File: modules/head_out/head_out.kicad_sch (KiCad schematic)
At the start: 27 parts, among them J1 AudioJack3, U1 MCP6002-xSN

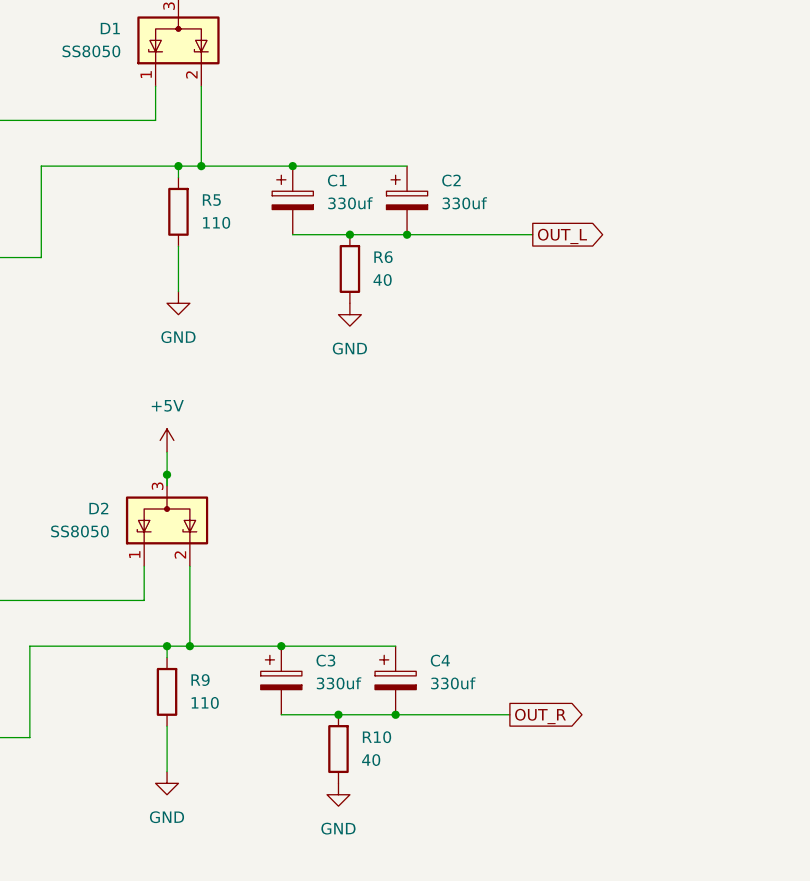
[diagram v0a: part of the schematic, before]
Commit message: Finished pcb_design of the head_out
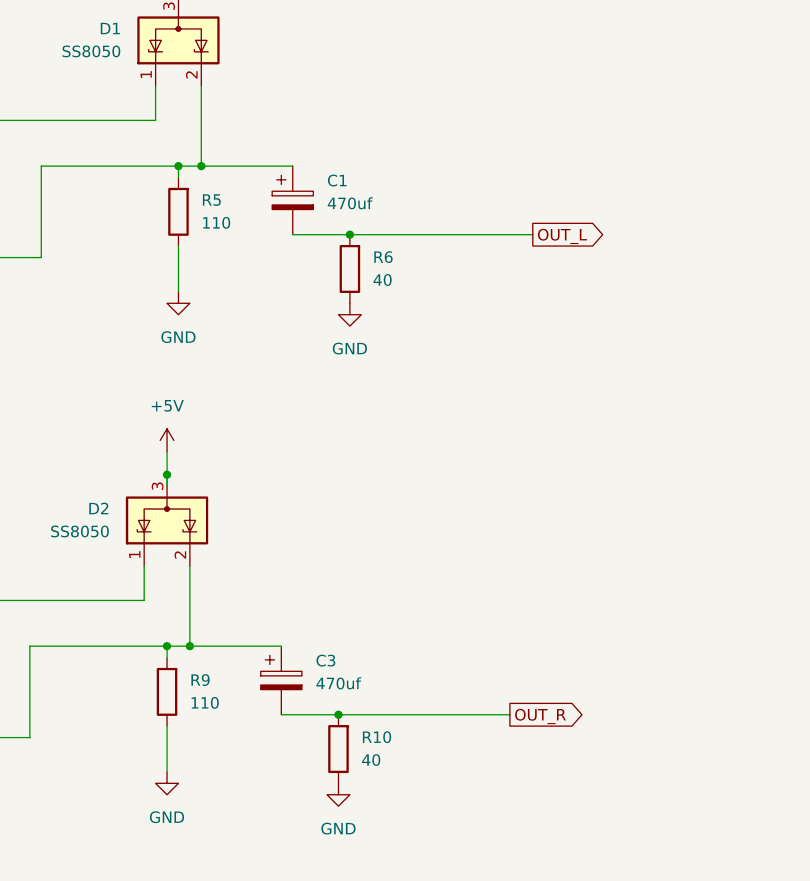
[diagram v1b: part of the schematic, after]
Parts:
- removed C2, C4: 330uf, Capacitor_SMD:CP_Elec_6.3x7.7, symbol Device:C_Polarized
- C1, C3: value 330uf -> 470uf
- RV1, RV2: footprint BreadModular_Pots:PanelHole_Potentiometer_RV09 -> BreadModular_Pots:Potentiometer_RV09
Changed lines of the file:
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@@
 	(paper "A4")
 	(junction
-		(at 153.67 143.51)
-		(diameter 0)
-		(color 0 0 0 0)
-	)
-	(junction
 		(at 82.55 80.01)
 		(diameter 0)
@@
 	)
 	(junction
-		(at 140.97 135.89)
-		(diameter 0)
-		(color 0 0 0 0)
-	)
-	(junction
 		(at 261.62 30.48)
 		(diameter 0)
@@
 	)
 	(junction
-		(at 142.24 82.55)
-		(diameter 0)
-		(color 0 0 0 0)
-	)
-	(junction
-		(at 154.94 90.17)
-		(diameter 0)
-		(color 0 0 0 0)
-	)
-	(junction
 		(at 148.59 90.17)
 		(diameter 0)
@@
 	(wire
 		(pts
-			(xy 153.67 143.51) (xy 166.37 143.51)
-		)
-		(stroke
-			(width 0)
-			(type default)
-		)
-	)
-	(wire
-		(pts
 			(xy 231.14 120.65) (xy 231.14 114.3)
 		)
@@
 	(wire
 		(pts
-			(xy 140.97 135.89) (xy 153.67 135.89)
-		)
-		(stroke
-			(width 0)
-			(type default)
-		)
-	)
-	(wire
-		(pts
-			(xy 147.32 143.51) (xy 153.67 143.51)
+			(xy 147.32 143.51) (xy 166.37 143.51)
 		)
 		(stroke
@@
 	(wire
 		(pts
-			(xy 142.24 82.55) (xy 154.94 82.55)
-		)
-		(stroke
-			(width 0)
-			(type default)
-		)
-	)
-	(wire
-		(pts
 			(xy 88.9 92.71) (xy 82.55 92.71)
 		)
@@
 	(wire
 		(pts
-			(xy 154.94 90.17) (xy 168.91 90.17)
-		)
-		(stroke
-			(width 0)
-			(type default)
-		)
-	)
-	(wire
-		(pts
 			(xy 266.7 30.48) (xy 269.24 30.48)
 		)
@@
 	(wire
 		(pts
-			(xy 148.59 90.17) (xy 154.94 90.17)
+			(xy 148.59 90.17) (xy 168.91 90.17)
 		)
 		(stroke
@@
 			)
 		)
-		(property "Value" "330uf"
+		(property "Value" "470uf"
 			(at 144.78 140.0809 0)
 			(effects
@@
 	)
 	(symbol
-		(lib_id "Device:C_Polarized")
-		(at 153.67 139.7 0)
-		(unit 1)
-		(exclude_from_sim no)
-		(in_bom yes)
-		(on_board yes)
-		(dnp no)
-		(fields_autoplaced yes)
-		(property "Reference" "C4"
-			(at 157.48 137.5409 0)
-			(effects
-				(font
-					(size 1.27 1.27)
-				)
-				(justify left)
-			)
-		)
-		(property "Value" "330uf"
-			(at 157.48 140.0809 0)
-			(effects
-				(font
-					(size 1.27 1.27)
-				)
-				(justify left)
-			)
-		)
-		(property "Footprint" "Capacitor_SMD:CP_Elec_6.3x7.7"
-			(at 154.6352 143.51 0)
-			(effects
-				(font
-					(size 1.27 1.27)
-				)
-				(hide yes)
-			)
-		)
-		(property "Datasheet" "~"
-			(at 153.67 139.7 0)
-			(effects
-				(font
-					(size 1.27 1.27)
-				)
-				(hide yes)
-			)
-		)
-		(property "Description" "Polarized capacitor"
-			(at 153.67 139.7 0)
-			(effects
-				(font
-					(size 1.27 1.27)
-				)
-				(hide yes)
-			)
-		)
-		(pin "1"
-		)
-		(pin "2"
-		)
-		(instances
-			(project "head_out"
-				(path "/b63493d3-5f6d-47e3-845b-87e7090fc1ab"
-					(reference "C4")
-					(unit 1)
-				)
-			)
-		)
-	)
-	(symbol
 		(lib_id "Connector:Conn_01x05_Pin")
 		(at 238.76 34.29 90)
@@
 			)
 		)
-		(property "Footprint" "BreadModular_Pots:PanelHole_Potentiometer_RV09"
+		(property "Footprint" "BreadModular_Pots:Potentiometer_RV09"
 			(at 41.91 140.97 0)
 			(effects
@@
 	)
 	(symbol
-		(lib_id "Device:C_Polarized")
-		(at 154.94 86.36 0)
-		(unit 1)
-		(exclude_from_sim no)
-		(in_bom yes)
-		(on_board yes)
-		(dnp no)
-		(fields_autoplaced yes)
-		(property "Reference" "C2"
-			(at 158.75 84.2009 0)
-			(effects
-				(font
-					(size 1.27 1.27)
-				)
-				(justify left)
-			)
-		)
-		(property "Value" "330uf"
-			(at 158.75 86.7409 0)
-			(effects
-				(font
-					(size 1.27 1.27)
-				)
-				(justify left)
-			)
-		)
-		(property "Footprint" "Capacitor_SMD:CP_Elec_6.3x7.7"
-			(at 155.9052 90.17 0)
-			(effects
-				(font
-					(size 1.27 1.27)
-				)
-				(hide yes)
-			)
-		)
-		(property "Datasheet" "~"
-			(at 154.94 86.36 0)
-			(effects
-				(font
-					(size 1.27 1.27)
-				)
-				(hide yes)
-			)
-		)
-		(property "Description" "Polarized capacitor"
-			(at 154.94 86.36 0)
-			(effects
-				(font
-					(size 1.27 1.27)
-				)
-				(hide yes)
-			)
-		)
-		(pin "1"
-		)
-		(pin "2"
-		)
-		(instances
-			(project "head_out"
-				(path "/b63493d3-5f6d-47e3-845b-87e7090fc1ab"
-					(reference "C2")
-					(unit 1)
-				)
-			)
-		)
-	)
-	(symbol
 		(lib_id "Amplifier_Operational:MCP6002-xSN")
 		(at 93.98 77.47 0)
@@
 			)
 		)
-		(property "Footprint" "BreadModular_Pots:PanelHole_Potentiometer_RV09"
+		(property "Footprint" "BreadModular_Pots:Potentiometer_RV09"
 			(at 43.18 87.63 0)
 			(effects
@@
 			)
 		)
-		(property "Value" "330uf"
+		(property "Value" "470uf"
 			(at 146.05 86.7409 0)
 			(effects

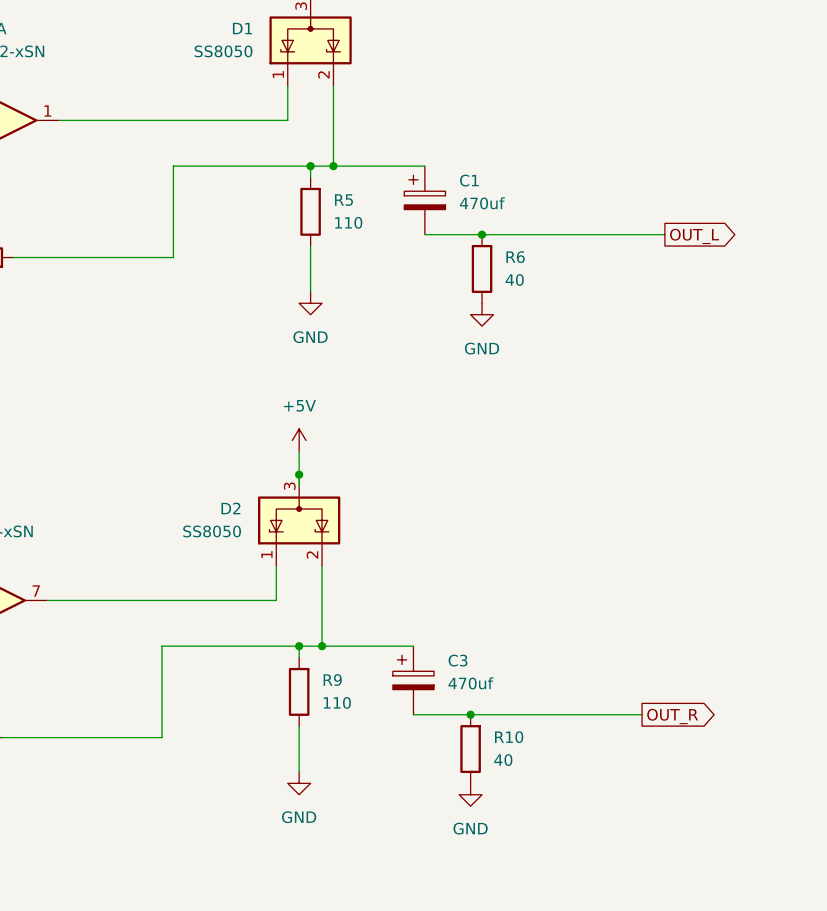
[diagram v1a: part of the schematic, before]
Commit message: Finialize the design based on actual wattage requirements.
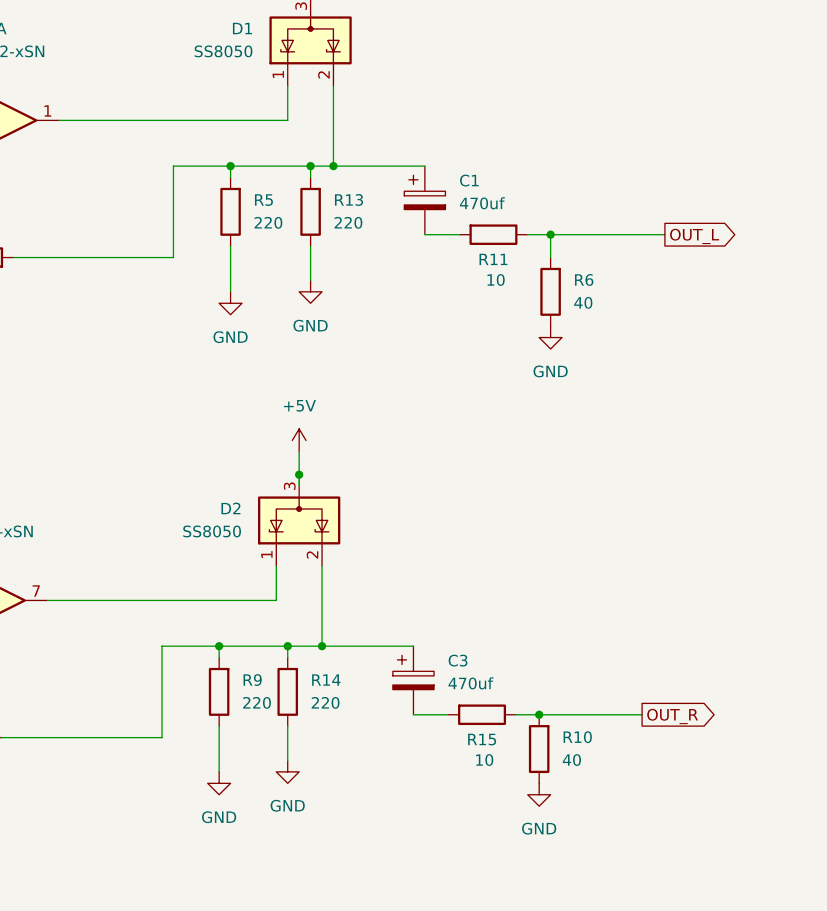
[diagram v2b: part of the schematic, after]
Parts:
- added R11, R15: 10, Resistor_SMD:R_1206_3216Metric, symbol Device:R
- added R13, R14: 220, Resistor_SMD:R_1206_3216Metric, symbol Device:R
- R5, R9: value 110 -> 220; footprint Resistor_SMD:R_0402_1005Metric -> Resistor_SMD:R_1206_3216Metric
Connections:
- net GND: now also R13.1, R14.1
- net OUT_L: now also R11.1; no longer C1.2
- net OUT_R: now also R15.1; no longer C3.2
- net at C3.1, D2.2 (K), R8.2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: now also R14.2
- net at C1.1, D1.2 (K), R1.2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: now also R13.2
- new net: C3.2, R15.2
- new net: C1.2, R11.2
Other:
- moved on the sheet: R10, R5, R6, R9

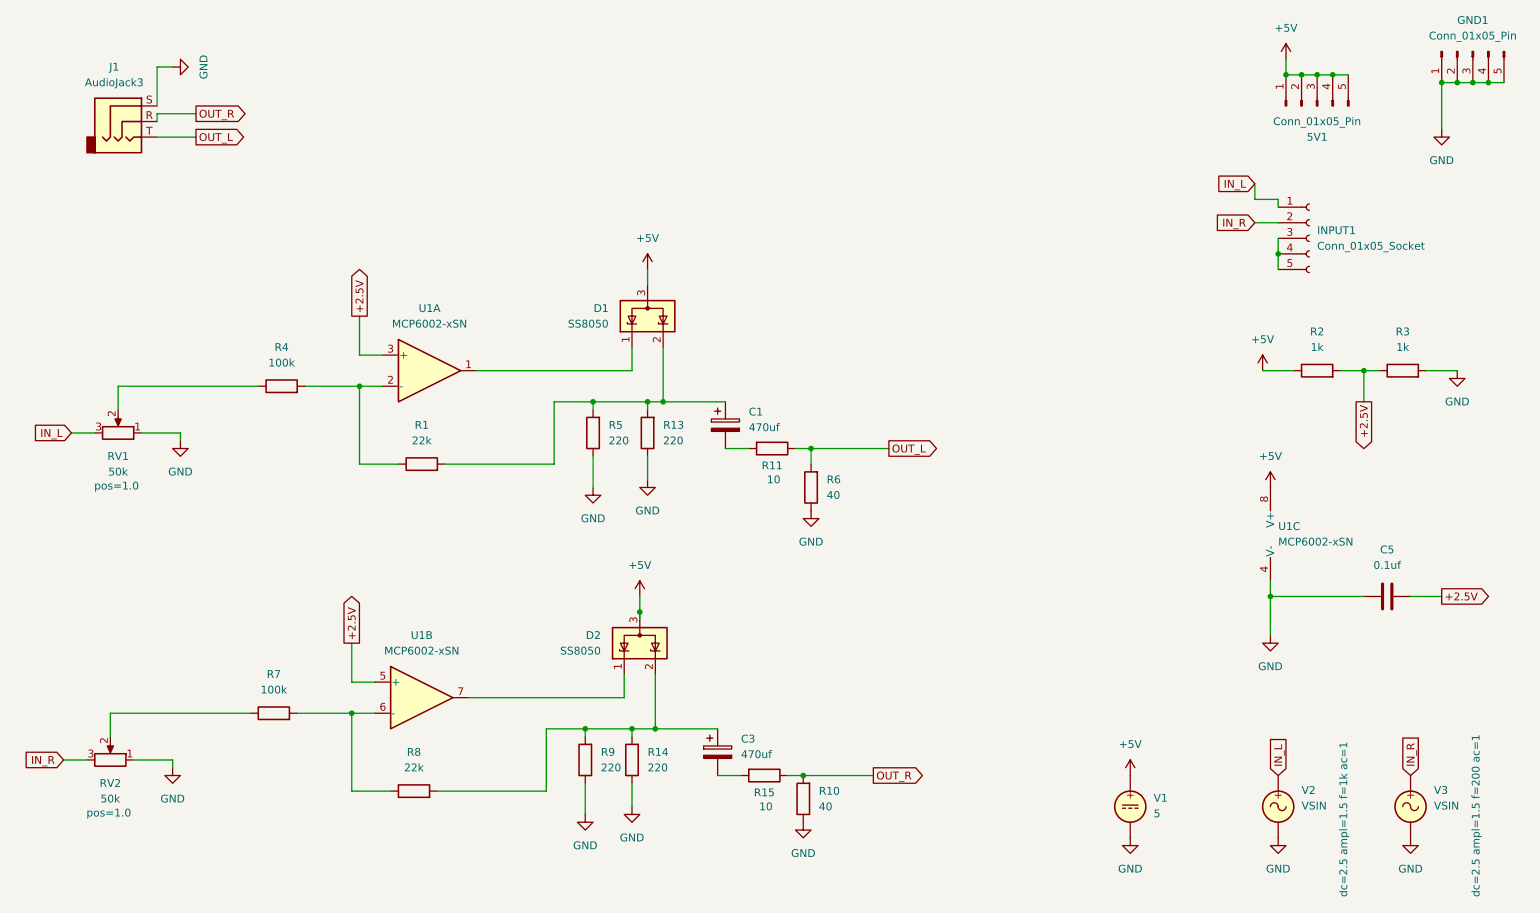
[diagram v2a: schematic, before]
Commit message: Finalize the head_out module.
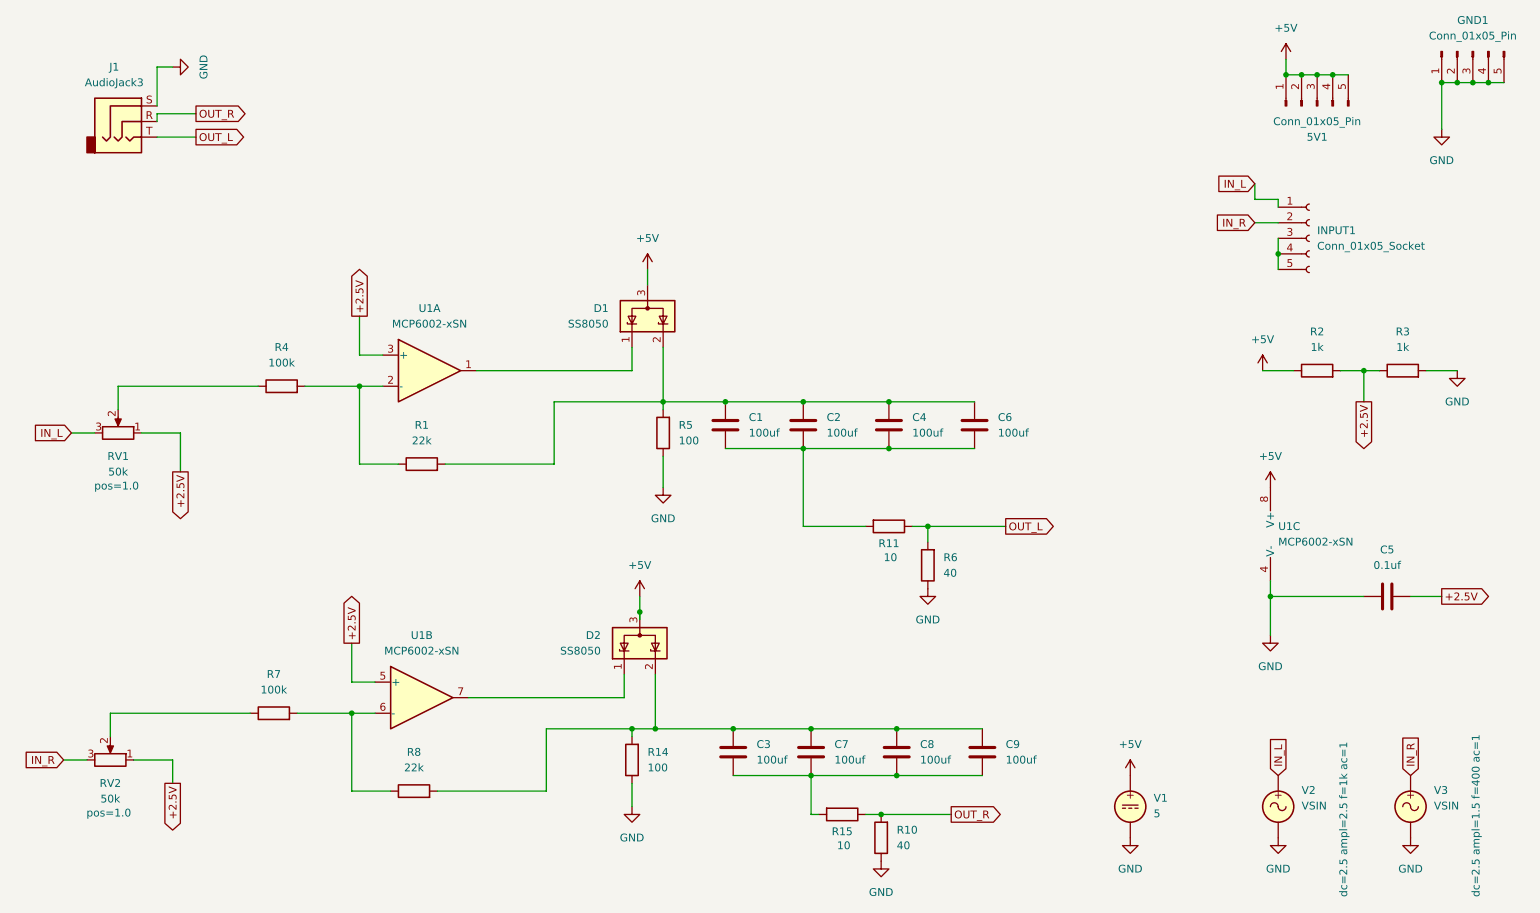
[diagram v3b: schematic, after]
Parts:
- removed C1, C3: 470uf, Capacitor_SMD:CP_Elec_6.3x7.7, symbol Device:C_Polarized
- removed R13, R9: 220, Resistor_SMD:R_1206_3216Metric, symbol Device:R
- added C1, C2, C3, C4, C6, C7, C8, C9: 100uf, Capacitor_SMD:C_1206_3216Metric, symbol Device:C
- R14, R5: value 220 -> 100
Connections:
- net +2.5V: now also RV1.1, RV2.1
- net GND: no longer RV1.1, RV2.1
- net at D2.2 (K), R14.2, R8.2: now also C3.1, C7.1, C8.1, C9.1
- net at R15.2: now also C3.2, C7.2, C8.2, C9.2
- net at D1.2 (K), R1.2, R5.2: now also C1.1, C2.1, C4.1, C6.1
- net at R11.2: now also C1.2, C2.2, C4.2, C6.2
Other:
- moved on the sheet: R10, R11, R15, R5, R6
